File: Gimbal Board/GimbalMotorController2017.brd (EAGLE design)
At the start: 83.4 x 72.1 mm, 125 parts, among them J1 SL03THROUGH_HOLE, J3 APP_2POS_CONFIG5V_HORIZ, Q7 MOSFET-PCHANNEL, Q8 MOSFET-PCHANNEL, Q9 MOSFET-NCHANNELAO3404A, U1 NUP4201MR6, U2 MAX3232D, U3 CSD18533Q5A, U4 CSD18533Q5A, U5 CSD18533Q5A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

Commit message: Board Updated for Board Review
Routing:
- net SDI: track 49.7 -> 48.9 mm
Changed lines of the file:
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@@
 <layers>
 <layer number="1" name="Top" color="4" fill="1" visible="yes" active="yes"/>
-<layer number="2" name="UpperMid" color="6" fill="1" visible="no" active="yes"/>
+<layer number="2" name="UpperMid" color="6" fill="1" visible="yes" active="yes"/>
 <layer number="3" name="Route3" color="4" fill="3" visible="no" active="no"/>
 <layer number="4" name="Route4" color="1" fill="4" visible="no" active="no"/>
@@
 <layer number="13" name="Route13" color="4" fill="5" visible="no" active="no"/>
 <layer number="14" name="Route14" color="1" fill="6" visible="no" active="no"/>
-<layer number="15" name="LowerMid" color="10" fill="1" visible="no" active="yes"/>
+<layer number="15" name="LowerMid" color="10" fill="1" visible="yes" active="yes"/>
 <layer number="16" name="Bottom" color="1" fill="1" visible="yes" active="yes"/>
 <layer number="17" name="Pads" color="2" fill="1" visible="yes" active="yes"/>
@@
 <wire x1="50.8" y1="3.81" x2="50.8" y2="4.80539375" width="0.254" layer="2"/>
 <wire x1="50.8" y1="4.80539375" x2="49.7078" y2="5.89759375" width="0.254" layer="2"/>
-<wire x1="49.7078" y1="5.89759375" x2="49.7078" y2="13.04436875" width="0.254" layer="2"/>
-<wire x1="49.7078" y1="13.04436875" x2="42.2176" y2="20.53456875" width="0.254" layer="2"/>
+<wire x1="49.7078" y1="5.89759375" x2="49.4538" y2="13.04436875" width="0.254" layer="2"/>
+<wire x1="49.4538" y1="13.04436875" x2="42.2176" y2="20.53456875" width="0.254" layer="2"/>
 <wire x1="42.2176" y1="27.8864" x2="42.164" y2="27.94" width="0.254" layer="2"/>
 <wire x1="42.2176" y1="20.53456875" x2="42.2176" y2="27.8864" width="0.254" layer="2"/>
@@
 <wire x1="47.32414375" y1="28.1698" x2="47.30434375" y2="28.15" width="0.254" layer="1"/>
 <wire x1="48.1552" y1="29.09754375" x2="48.1552" y2="28.363225" width="0.254" layer="1"/>
-<wire x1="47.961775" y1="28.1698" x2="47.0698" y2="28.1698" width="0.254" layer="1"/>
+<wire x1="47.32414375" y1="28.1698" x2="47.0698" y2="28.1698" width="0.254" layer="1"/>
 <wire x1="47.0698" y1="28.1698" x2="47.05" y2="28.15" width="0.254" layer="1"/>
 </signal>
@@
 <wire x1="73.8615" y1="45.43425" x2="73.8615" y2="47.01375" width="0.254" layer="1"/>
 <wire x1="73.50425" y1="47.371" x2="73.8615" y2="47.01375" width="0.254" layer="1"/>
-<wire x1="54.55" y1="19.65" x2="55.661" y2="19.4976" width="0.254" layer="1"/>
-<wire x1="55.661" y1="19.4976" x2="56.1594" y2="19.4056" width="0.254" layer="1"/>
-<wire x1="56.1594" y1="19.4056" x2="58.582" y2="19.65" width="0.254" layer="1"/>
+<wire x1="54.55" y1="19.65" x2="55.6102" y2="19.523" width="0.254" layer="1"/>
+<wire x1="55.6102" y1="19.523" x2="56.1086" y2="19.3802" width="0.254" layer="1"/>
+<wire x1="56.1086" y1="19.3802" x2="58.582" y2="19.65" width="0.254" layer="1"/>
 <wire x1="58.582" y1="19.65" x2="59.5122" y2="19.5072" width="0.254" layer="1"/>
 <via x="59.5122" y="19.5072" extent="1-16" drill="0.35"/>

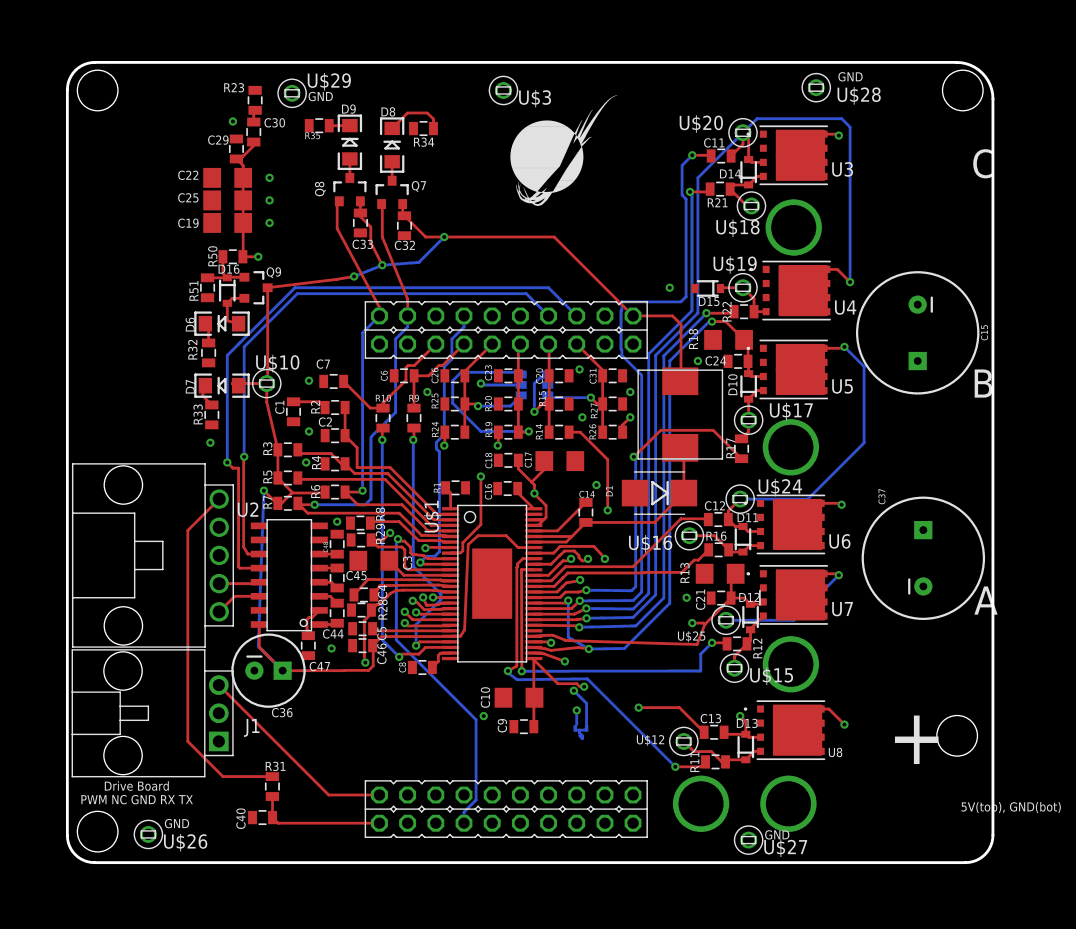
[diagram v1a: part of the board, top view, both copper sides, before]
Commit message: Fixed certain silkscreen issues and routing
LED's are now fully labelled and in easy to see places
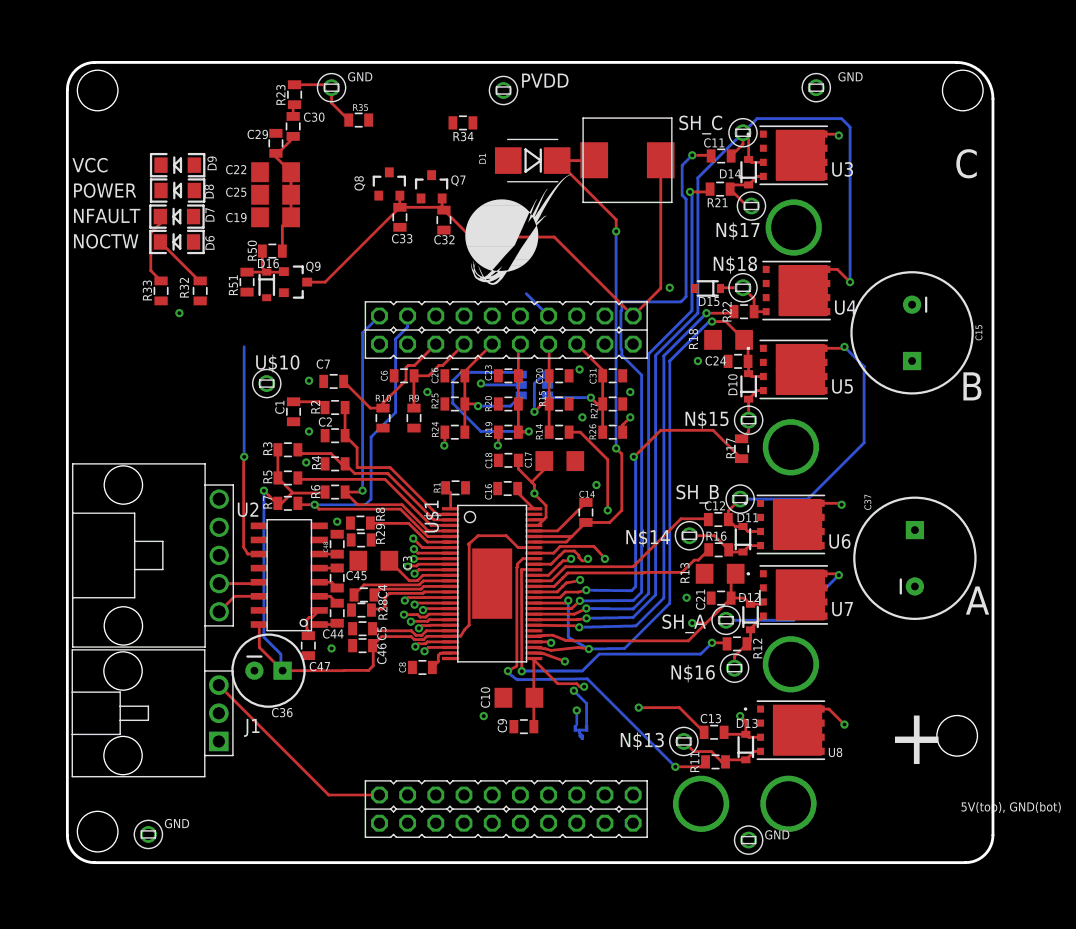
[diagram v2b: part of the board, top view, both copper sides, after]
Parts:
- removed C40: .015u, SparkFun-Passives:0805
- removed R31: 100, SparkFun-Passives:0805
- moved D1 32.1 mm to (54.5, 63.5)
- moved U$14 23.4 mm to (63.0, 63.6), turned to 0 degrees
- moved D8 19.8 mm to (22.4, 60.8), turned to 180 degrees
- moved D7 15.8 mm to (22.4, 58.5)
- moved D9 15.7 mm to (22.4, 63.1), turned to 180 degrees
- moved R33 12.1 mm to (21.0, 51.8)
- moved D6 8.41 mm to (22.4, 56.2)
- moved U$9 8.19 mm to (48.4, 51.5)
- moved R32 5.64 mm to (24.5, 51.8)
- moved C19 4.35 mm to (31.3, 58.4)
- moved C22 4.35 mm to (31.3, 62.5)
- moved C25 4.35 mm to (31.3, 60.5)
- moved R35 3.59 mm to (38.8, 67.2)
- moved Q8 3.59 mm to (41.5, 61.4)
- moved Q9 3.59 mm to (33.0, 52.6)
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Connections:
- removed net N$34: R31.2, U$4.1
- net GND: no longer C40.2
- net PWM_IN: no longer C40.1, R31.1
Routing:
- net UART_RX: track 57.2 -> 0.00 mm, vias 1 -> 0
- net SDI: track 48.9 -> 3.45 mm
- net DC_CAL: track 44.2 -> 3.39 mm
- net NSCS: track 42.7 -> 3.70 mm
- net N$34: track 31.9 -> 0.00 mm
- net SDO: track 34.8 -> 3.32 mm
- net EN_GATE: track 37.0 -> 8.25 mm, vias 1 -> 0
- net UART_TX: track 50.1 -> 22.7 mm
- net N$31: track 23.0 -> 49.8 mm, vias 0 -> 2
- net INH_B: track 27.4 -> 2.54 mm
- net INL_A: track 27.8 -> 3.30 mm
- net N$11: track 26.3 -> 2.49 mm, vias 2 -> 1
- net VCC: track 164.8 -> 141.2 mm, vias 5 -> 2
- net SCLK: track 27.6 -> 3.96 mm
- net INH_A: track 27.6 -> 4.24 mm
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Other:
- board text added: "N$13"
- board text added: "N$14"
- board text added: "N$15"
- board text added: "N$16"
- board text added: "N$17"
- board text added: "N$18"
- board text added: "NFAULT"
- board text added: "NOCTW"
- board text added: "POWER"
- board text added: "PVDD"
- board text added: "SH_A"
- board text added: "SH_B"
- board text added: "SH_C"
- board text added: "VCC"
- board text removed: "Drive Board PWM NC GND RX TX"

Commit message: Changed Resistor values for 15v to 3.3v conversion.
Changed resistor values for 15v to 3.3v conversion. Bumped up the magnitude by 10x per board review #1 suggestions.
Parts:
- R14, R19, R24, R26: value 13.2k -> 184k
- R15, R20, R25, R27: value 4.99k -> 50k
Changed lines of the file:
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@@
 <?xml version="1.0" encoding="utf-8"?>
 <!DOCTYPE eagle SYSTEM "eagle.dtd">
-<eagle version="8.3.2">
+<eagle version="8.5.1">
 <drawing>
 <settings>
-<setting alwaysvectorfont="yes"/>
+<setting alwaysvectorfont="no"/>
 <setting keepoldvectorfont="yes"/>
 <setting verticaltext="up"/>
@@
 <param name="dpMaxLengthDifference" value="10mm"/>
 <param name="dpGapFactor" value="2.5"/>
-<param name="checkGrid" value="0"/>
 <param name="checkAngle" value="0"/>
 <param name="checkFont" value="1"/>
 <param name="checkRestrict" value="1"/>
+<param name="checkStop" value="0"/>
+<param name="checkValues" value="0"/>
 <param name="useDiameter" value="13"/>
 <param name="maxErrors" value="50"/>
@@
 <attribute name="VALUE" x="71.08825" y="19.78025" size="0.4064" layer="27" font="vector" rot="R270"/>
 </element>
-<element name="R14" library="SparkFun-Passives" package="0805" value="13.2k" x="56.8325" y="39.0525" smashed="yes" rot="R180">
+<element name="R14" library="SparkFun-Passives" package="0805" value="184k" x="56.8325" y="39.0525" smashed="yes" rot="R180">
 <attribute name="NAME" x="54.737" y="39.8145" size="0.6096" layer="25" font="vector" rot="R270"/>
 <attribute name="VALUE" x="57.0865" y="40.1955" size="0.4064" layer="27" font="vector" rot="R180"/>
 </element>
-<element name="R15" library="SparkFun-Passives" package="0805" value="4.99k" x="56.8325" y="41.5925" smashed="yes">
+<element name="R15" library="SparkFun-Passives" package="0805" value="50k" x="56.8325" y="41.5925" smashed="yes">
 <attribute name="NAME" x="55.626" y="41.3385" size="0.6096" layer="25" font="vector" rot="R90"/>
 <attribute name="VALUE" x="55.8165" y="42.2275" size="0.4064" layer="27" font="vector"/>
@@
 <attribute name="VALUE" x="74.168" y="37.81425" size="0.4064" layer="27" font="vector" rot="R270"/>
 </element>
-<element name="R19" library="SparkFun-Passives" package="0805" value="13.2k" x="52.2605" y="39.0525" smashed="yes">
+<element name="R19" library="SparkFun-Passives" package="0805" value="184k" x="52.2605" y="39.0525" smashed="yes">
 <attribute name="NAME" x="50.8" y="38.5445" size="0.6096" layer="25" font="vector" rot="R90"/>
 <attribute name="VALUE" x="50.9905" y="39.9415" size="0.4064" layer="27" font="vector"/>
@@
 <attribute name="VALUE" x="38.1" y="42.2275" size="0.4064" layer="27" font="vector" rot="R270"/>
 </element>
-<element name="R20" library="SparkFun-Passives" package="0805" value="4.99k" x="52.2605" y="41.5925" smashed="yes" rot="R180">
+<element name="R20" library="SparkFun-Passives" package="0805" value="50k" x="52.2605" y="41.5925" smashed="yes" rot="R180">
 <attribute name="NAME" x="50.165" y="42.3545" size="0.6096" layer="25" font="vector" rot="R270"/>
 <attribute name="VALUE" x="52.5145" y="42.7355" size="0.4064" layer="27" font="vector" rot="R180"/>
@@
 <attribute name="VALUE" x="34.13125" y="68.961" size="0.4064" layer="27" font="vector" rot="R90"/>
 </element>
-<element name="R24" library="SparkFun-Passives" package="0805" value="13.2k" x="47.4345" y="39.0525" smashed="yes">
+<element name="R24" library="SparkFun-Passives" package="0805" value="184k" x="47.4345" y="39.0525" smashed="yes">
 <attribute name="NAME" x="45.974" y="38.5445" size="0.6096" layer="25" font="vector" rot="R90"/>
 <attribute name="VALUE" x="46.1645" y="39.9415" size="0.4064" layer="27" font="vector"/>
 </element>
-<element name="R25" library="SparkFun-Passives" package="0805" value="4.99k" x="47.4345" y="41.5925" smashed="yes" rot="R180">
+<element name="R25" library="SparkFun-Passives" package="0805" value="50k" x="47.4345" y="41.5925" smashed="yes" rot="R180">
 <attribute name="NAME" x="45.339" y="42.6085" size="0.6096" layer="25" font="vector" rot="R270"/>
 <attribute name="VALUE" x="47.6885" y="42.7355" size="0.4064" layer="27" font="vector" rot="R180"/>
 </element>
-<element name="R26" library="SparkFun-Passives" package="0805" value="13.2k" x="61.6585" y="39.0525" smashed="yes" rot="R180">
+<element name="R26" library="SparkFun-Passives" package="0805" value="184k" x="61.6585" y="39.0525" smashed="yes" rot="R180">
 <attribute name="NAME" x="59.563" y="39.8145" size="0.6096" layer="25" font="vector" rot="R270"/>
 <attribute name="VALUE" x="62.1665" y="40.1955" size="0.4064" layer="27" font="vector" rot="R180"/>
 </element>
-<element name="R27" library="SparkFun-Passives" package="0805" value="4.99k" x="61.6585" y="41.5925" smashed="yes">
+<element name="R27" library="SparkFun-Passives" package="0805" value="50k" x="61.6585" y="41.5925" smashed="yes">
 <attribute name="NAME" x="59.69" y="41.7195" size="0.6096" layer="25" font="vector" rot="R270"/>
 <attribute name="VALUE" x="60.6425" y="42.4815" size="0.4064" layer="27" font="vector"/>

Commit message: Changed Fets Around and redid routing
Fets are now ABC, instead of CBA. This made for easier routing. Silkscreen is updated and the LED's are properly labelled. FET models are still unchanged. Routing has been cleaned up to the best of my ability. Will try and clean up in future work times.
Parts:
- moved R12 40.9 mm to (73.1, 60.9)
- moved R13 40.9 mm to (71.6, 67.2)
- moved U7 40.9 mm to (78.2, 65.3)
- moved C13 40.9 mm to (71.1, 52.9)
- moved C21 40.9 mm to (71.7, 65.0)
- moved D12 40.9 mm to (74.3, 63.3)
- moved D13 40.9 mm to (73.9, 51.6)
- moved R11 40.9 mm to (71.2, 50.2)
- moved U$12 40.9 mm to (68.3, 52.1)
- moved U$15 40.9 mm to (72.9, 58.7)
- moved U$25 40.9 mm to (72.1, 63.0)
- moved U8 40.9 mm to (78.0, 53.1)
- moved U$5 40.6 mm to (106.2, 62.7)
- moved U$20 40.4 mm to (72.1, 25.7)
- moved D14 40.4 mm to (72.6, 22.1)
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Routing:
- net NSCS: track 3.70 -> 79.5 mm
- net VCC: track 141.2 -> 204.6 mm, vias 2 -> 6
- net SDI: track 3.45 -> 66.1 mm
- net UART_RX: track 0.00 -> 55.5 mm, vias 0 -> 1
- net SDO: track 3.32 -> 58.3 mm
- net N$21: track 58.3 -> 15.0 mm, vias 2 -> 0
- net GH_C: track 50.9 -> 15.5 mm, vias 2 -> 0
- net N$27: track 0.00 -> 34.8 mm
- net N$26: track 0.00 -> 34.3 mm
- net N$30: track 5.76 -> 39.7 mm, vias 0 -> 2
- net DC_CAL: track 3.39 -> 37.1 mm, vias 1 -> 2
- net INH_A: track 4.24 -> 35.3 mm
- net INL_C: track 2.97 -> 33.8 mm
- net INH_C: track 3.66 -> 33.8 mm
- net INL_B: track 4.40 -> 34.5 mm
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
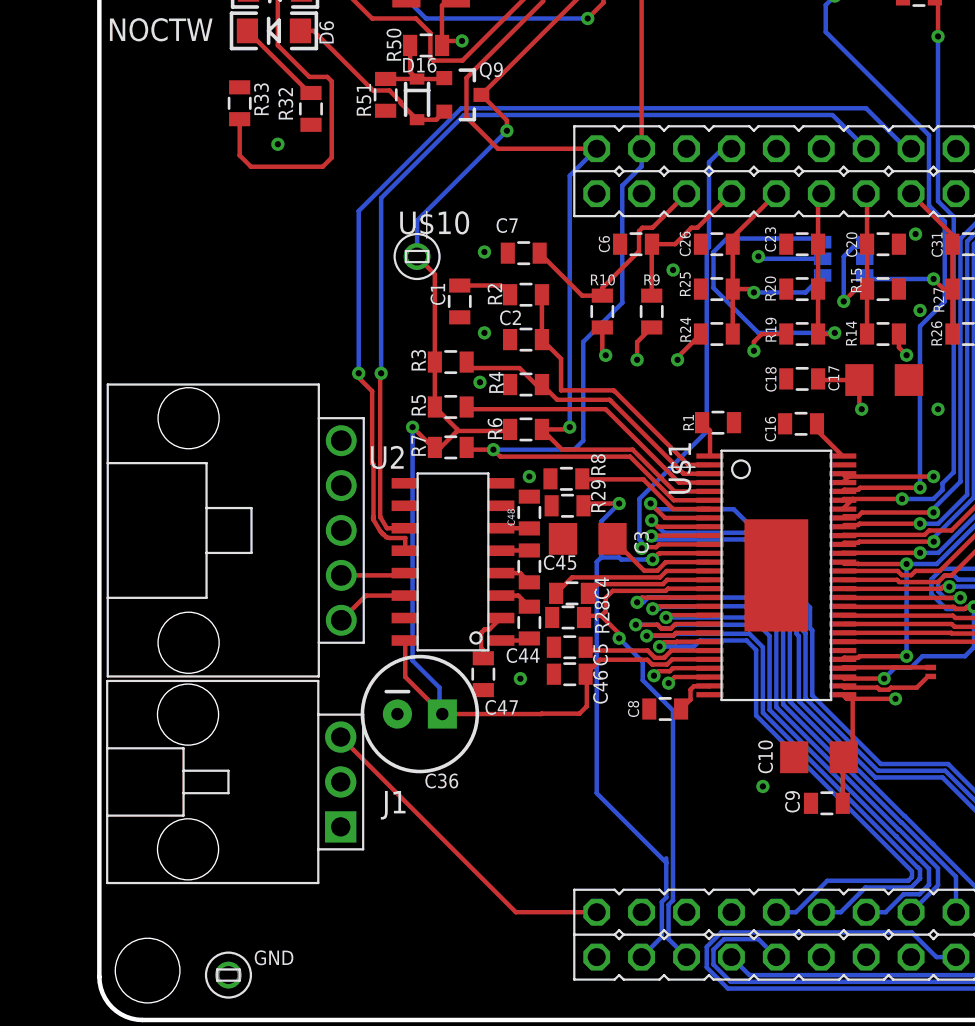
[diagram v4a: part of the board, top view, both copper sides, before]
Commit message: Moved Max232 to avoid bridging with SL connectors
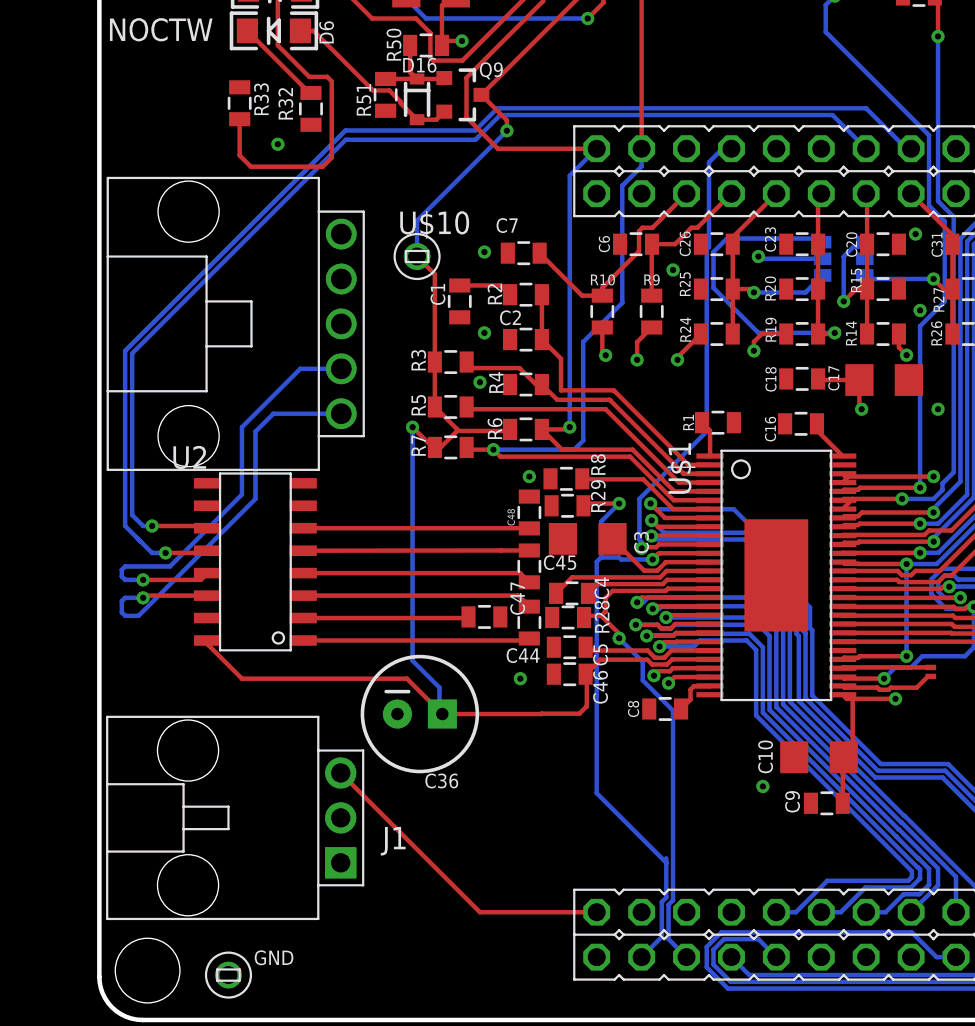
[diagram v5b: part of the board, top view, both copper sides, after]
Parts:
- moved U$4 11.7 mm to (26.2, 39.6)
- moved U2 11.2 mm to (21.3, 26.2)
- moved C47 3.24 mm to (34.3, 23.1), turned to 0 degrees
- moved J1 2.03 mm to (26.2, 11.7)
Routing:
- net 232_RX: track 3.67 -> 24.8 mm, vias 0 -> 1
- net 232_TX: track 4.20 -> 25.1 mm, vias 0 -> 1
- net UART_TX: track 50.0 -> 61.6 mm
- net N$45: track 1.62 -> 12.8 mm
- net N$43: track 1.83 -> 13.0 mm
- net N$42: track 1.88 -> 13.1 mm
- net N$40: track 1.67 -> 12.8 mm
- net N$44: track 1.62 -> 12.8 mm
- net UART_RX: track 55.5 -> 66.6 mm
- net VCC: track 204.6 -> 214.7 mm
- net N$46: track 2.94 -> 9.38 mm
- net PWM_IN_NO_FILTER: track 18.6 -> 17.7 mm

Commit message: Added new FET package, reorganized schematic to further clean up the labeling
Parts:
- removed U3, U4, U5, U6, U7, U8: CSD18533Q5A, CSD18533:DQJ8
- added Q1, Q2, Q3, Q4, Q5, Q6: Q_IRF7437SMD, R6020ENJTL ROHM D2PACK:D2PACK
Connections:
- net GND: now also Q6.2; no longer U4.3
- net N$13: now also Q2.1; no longer U8.4
- net N$14: now also Q3.1; no longer U6.4
- net N$15: now also Q4.1; no longer U5.4
- net N$16: now also Q1.1; no longer U7.4
- net N$17: now also Q5.1; no longer U3.4
- net N$18: now also Q6.1; no longer U4.4
- net PVDD: now also Q2.TAB, Q3.TAB, Q5.TAB; no longer U3.8, U6.8, U8.8
- net SH_A: now also Q1.TAB, Q2.2; no longer U7.8, U8.3
- net SH_B: now also Q3.2, Q4.TAB; no longer U5.8, U6.3
- net SH_C: now also Q5.2, Q6.TAB; no longer U3.3, U4.8
- net SL_A: now also Q1.2; no longer U7.3
- net SL_B: now also Q4.2; no longer U5.3
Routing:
- net PVDD: track 67.3 -> 60.8 mm, vias 8 -> 5
- net SH_B: track 74.2 -> 71.4 mm
- net SH_A: track 84.6 -> 82.3 mm
- net SH_C: track 89.3 -> 87.3 mm
- net N$16: track 5.78 -> 4.14 mm
- net N$18: track 5.72 -> 4.62 mm
- net SL_B: track 54.2 -> 53.1 mm
- net N$14: track 7.26 -> 6.25 mm
- net N$17: track 6.03 -> 5.47 mm
- net N$15: track 5.48 -> 4.92 mm
- net N$13: track 8.07 -> 7.51 mm
